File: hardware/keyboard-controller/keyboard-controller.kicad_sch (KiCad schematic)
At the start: 17 parts, among them J1 Debug_Pins, SW1 RESET, SW2 MODE_SEL, U1 Pico, U2 MCP4921

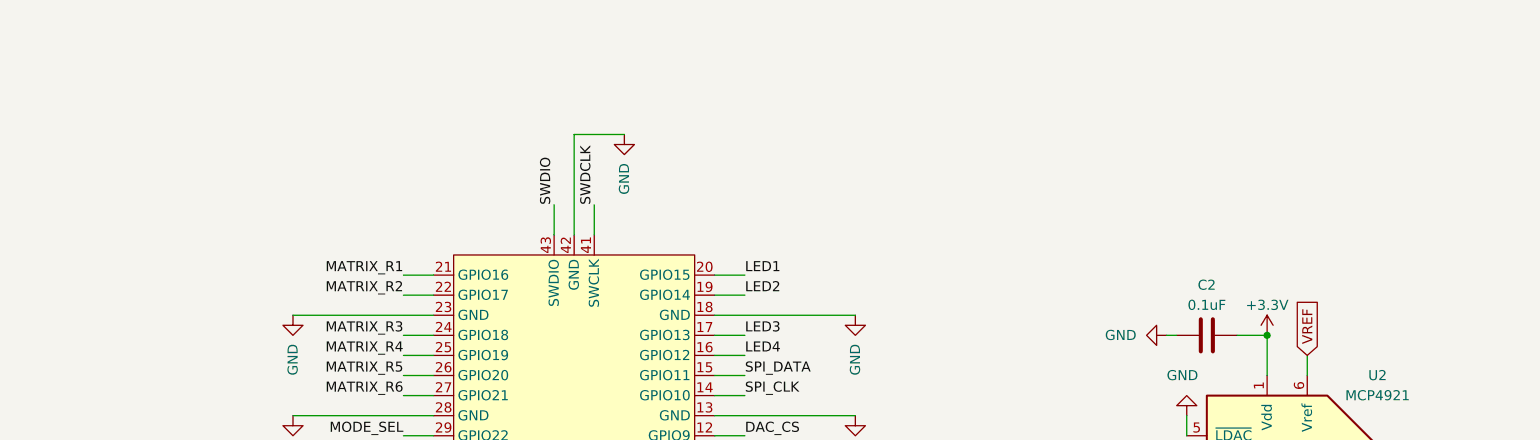
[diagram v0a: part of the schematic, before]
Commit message: Completed schematic rev1. Started placing pcb
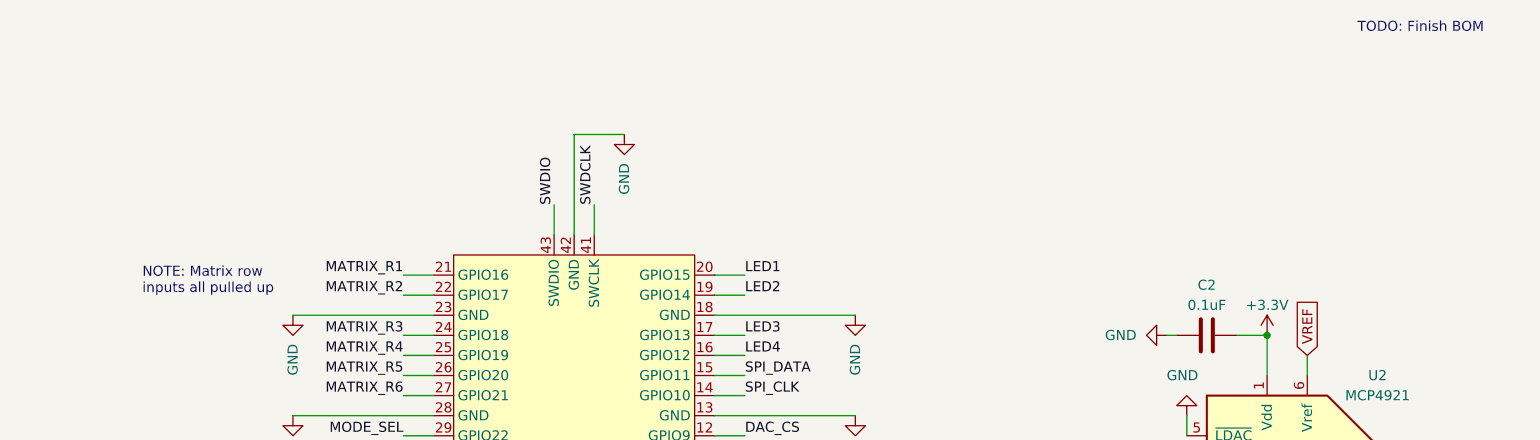
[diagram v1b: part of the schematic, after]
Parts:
- D1, D2, D3, D4, D5: footprint (none) -> LED_THT:LED_D5.0mm
- R1, R2, R3, R4, R5: footprint (none) -> Royal_Ohm_Resistors:R_Axial_DIN0207_L6.8mm_D2.5mm_P10.16mm_Horizontal
- SW1: footprint (none) -> Button_Switch_THT:SW_PUSH_6mm; Manufacturer (none) -> WEALTH METAL; Manufacturer Part No. (none) -> Tact Switch 6x6mm 5mm; Supplier Part No. (none) -> A-5127
- SW2: footprint (none) -> Wealth_Metal_Switches:Slide_Switch_SPDT_SS12F44G5; Manufacturer (none) -> WEALTH METAL; Manufacturer Part No. (none) -> SS12F44G5; Supplier Part No. (none) -> A-659
- U1: footprint RPi_Pico:RPi_Pico_SMD_TH -> MCU_RaspberryPi_and_Boards:RPi_Pico_SMD_TH
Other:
- note added: "NOTE: Matrix row inputs all pulled up"
- note added: "TODO: Finish BOM"

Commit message: Completed initial pcb design
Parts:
- added H1, H2, H3, H4: MountingHole, MountingHole:MountingHole_3.2mm_M3, symbol Mechanical:MountingHole
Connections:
- net GND: now also J1.4 (Pin_4); no longer J1.2 (Pin_2)
- net SERCLK: now also J1.2 (Pin_2); no longer J1.4 (Pin_4)
- net SERDATA: now also J1.1 (Pin_1); no longer J1.5 (Pin_5)
- net SWDCLK: now also J1.3 (Pin_3); no longer J1.1 (Pin_1)
- net SWDIO: now also J1.5 (Pin_5); no longer J1.3 (Pin_3)
- net +3V3 renamed +3.3V

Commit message: Added more text detail to PCB. Completed more of BOM
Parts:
- D1: Manufacturer (none) -> Tayda; Manufacturer Part No. (none) -> LED 5mm Green; Supplier Part No. (none) -> A-1553
- D2, D3, D4, D5: Manufacturer (none) -> Cree LED; Manufacturer Part No. (none) -> C503B-RAN-CZ0C0AA1; Notes (none) -> Standard 5mm Red LED; Supplier Tayda -> Mouser; Supplier Part No. (none) -> 941-C503BRANCZ0C0AA1
- H1, H2, H3, H4: Manufacturer (none) -> N/A; Manufacturer Part No. (none) -> N/A; Notes (none) -> N/A; Supplier (none) -> N/A; Supplier Part No. (none) -> N/A
- J1: Manufacturer (none) -> GTK; Manufacturer Part No. (none) -> PHSS05G10; Supplier Part No. (none) -> A-5775
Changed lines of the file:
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@@
+      (effects (font (size 1.27 1.27)) hide)
+    )
+    (property "Manufacturer" "Tayda" (id 5) (at 111.76 119.38 0)
+      (effects (font (size 1.27 1.27)) hide)
+    )
+    (property "Manufacturer Part No." "LED 5mm Green" (id 6) (at 111.76 119.38 0)
+      (effects (font (size 1.27 1.27)) hide)
+    )
+    (property "Supplier Part No." "A-1553" (id 7) (at 111.76 119.38 0)
       (effects (font (size 1.27 1.27)) hide)
     )
@@
       (effects (font (size 1.27 1.27)) hide)
     )
+    (property "Manufacturer" "N/A" (id 4) (at 254 148.59 0)
+      (effects (font (size 1.27 1.27)) hide)
+    )
+    (property "Manufacturer Part No." "N/A" (id 5) (at 254 148.59 0)
+      (effects (font (size 1.27 1.27)) hide)
+    )
+    (property "Notes" "N/A" (id 6) (at 254 148.59 0)
+      (effects (font (size 1.27 1.27)) hide)
+    )
+    (property "Supplier" "N/A" (id 7) (at 254 148.59 0)
+      (effects (font (size 1.27 1.27)) hide)
+    )
+    (property "Supplier Part No." "N/A" (id 8) (at 254 148.59 0)
+      (effects (font (size 1.27 1.27)) hide)
+    )
   )
   (symbol (lib_id "Mechanical:MountingHole") (at 232.41 148.59 0) (unit 1)
@@
       (effects (font (size 1.27 1.27)) hide)
     )
+    (property "Manufacturer" "N/A" (id 4) (at 232.41 148.59 0)
+      (effects (font (size 1.27 1.27)) hide)
+    )
+    (property "Manufacturer Part No." "N/A" (id 5) (at 232.41 148.59 0)
+      (effects (font (size 1.27 1.27)) hide)
+    )
+    (property "Notes" "N/A" (id 6) (at 232.41 148.59 0)
+      (effects (font (size 1.27 1.27)) hide)
+    )
+    (property "Supplier" "N/A" (id 7) (at 232.41 148.59 0)
+      (effects (font (size 1.27 1.27)) hide)
+    )
+    (property "Supplier Part No." "N/A" (id 8) (at 232.41 148.59 0)
+      (effects (font (size 1.27 1.27)) hide)
+    )
   )
   (symbol (lib_id "Device:R") (at 124.46 135.89 90) (unit 1)
@@
       (effects (font (size 1.27 1.27)) hide)
     )
-    (property "Supplier" "Tayda" (id 4) (at 113.03 167.64 0)
+    (property "Supplier" "Mouser" (id 4) (at 113.03 167.64 0)
+      (effects (font (size 1.27 1.27)) hide)
+    )
+    (property "Manufacturer" "Cree LED" (id 5) (at 113.03 167.64 0)
+      (effects (font (size 1.27 1.27)) hide)
+    )
+    (property "Manufacturer Part No." "C503B-RAN-CZ0C0AA1 " (id 6) (at 113.03 167.64 0)
+      (effects (font (size 1.27 1.27)) hide)
+    )
+    (property "Notes" "Standard 5mm Red LED" (id 7) (at 113.03 167.64 0)
+      (effects (font (size 1.27 1.27)) hide)
+    )
+    (property "Supplier Part No." "941-C503BRANCZ0C0AA1 " (id 8) (at 113.03 167.64 0)
       (effects (font (size 1.27 1.27)) hide)
     )
@@
       (effects (font (size 1.27 1.27)) hide)
     )
+    (property "Manufacturer" "N/A" (id 4) (at 254 158.75 0)
+      (effects (font (size 1.27 1.27)) hide)
+    )
+    (property "Manufacturer Part No." "N/A" (id 5) (at 254 158.75 0)
+      (effects (font (size 1.27 1.27)) hide)
+    )
+    (property "Notes" "N/A" (id 6) (at 254 158.75 0)
+      (effects (font (size 1.27 1.27)) hide)
+    )
+    (property "Supplier" "N/A" (id 7) (at 254 158.75 0)
+      (effects (font (size 1.27 1.27)) hide)
+    )
+    (property "Supplier Part No." "N/A" (id 8) (at 254 158.75 0)
+      (effects (font (size 1.27 1.27)) hide)
+    )
   )
   (symbol (lib_id "power:GND") (at 130.81 96.52 0) (unit 1)
@@
       (effects (font (size 1.27 1.27)) hide)
     )
+    (property "Manufacturer" "N/A" (id 4) (at 232.41 158.75 0)
+      (effects (font (size 1.27 1.27)) hide)
+    )
+    (property "Manufacturer Part No." "N/A" (id 5) (at 232.41 158.75 0)
+      (effects (font (size 1.27 1.27)) hide)
+    )
+    (property "Notes" "N/A" (id 6) (at 232.41 158.75 0)
+      (effects (font (size 1.27 1.27)) hide)
+    )
+    (property "Supplier" "N/A" (id 7) (at 232.41 158.75 0)
+      (effects (font (size 1.27 1.27)) hide)
+    )
+    (property "Supplier Part No." "N/A" (id 8) (at 232.41 158.75 0)
+      (effects (font (size 1.27 1.27)) hide)
+    )
   )
   (symbol (lib_id "power:GND") (at 187.96 57.15 0) (mirror y) (unit 1)
@@
       (effects (font (size 1.27 1.27)) hide)
     )
-    (property "Supplier" "Tayda" (id 4) (at 113.03 184.15 0)
+    (property "Supplier" "Mouser" (id 4) (at 113.03 184.15 0)
+      (effects (font (size 1.27 1.27)) hide)
+    )
+    (property "Manufacturer" "Cree LED" (id 5) (at 113.03 184.15 0)
+      (effects (font (size 1.27 1.27)) hide)
+    )
+    (property "Manufacturer Part No." "C503B-RAN-CZ0C0AA1 " (id 6) (at 113.03 184.15 0)
+      (effects (font (size 1.27 1.27)) hide)
+    )
+    (property "Notes" "Standard 5mm Red LED" (id 7) (at 113.03 184.15 0)
+      (effects (font (size 1.27 1.27)) hide)
+    )
+    (property "Supplier Part No." "941-C503BRANCZ0C0AA1 " (id 8) (at 113.03 184.15 0)
       (effects (font (size 1.27 1.27)) hide)
     )
@@
       (effects (font (size 1.27 1.27)) hide)
     )
-    (property "Supplier" "Tayda" (id 4) (at 111.76 151.13 0)
+    (property "Supplier" "Mouser" (id 4) (at 111.76 151.13 0)
+      (effects (font (size 1.27 1.27)) hide)
+    )
+    (property "Manufacturer" "Cree LED" (id 5) (at 111.76 151.13 0)
+      (effects (font (size 1.27 1.27)) hide)
+    )
+    (property "Manufacturer Part No." "C503B-RAN-CZ0C0AA1 " (id 6) (at 111.76 151.13 0)
+      (effects (font (size 1.27 1.27)) hide)
+    )
+    (property "Notes" "Standard 5mm Red LED" (id 7) (at 111.76 151.13 0)
+      (effects (font (size 1.27 1.27)) hide)
+    )
+    (property "Supplier Part No." "941-C503BRANCZ0C0AA1 " (id 8) (at 111.76 151.13 0)
       (effects (font (size 1.27 1.27)) hide)
     )
@@
       (effects (font (size 1.27 1.27)) hide)
     )
+    (property "Manufacturer" "GTK" (id 5) (at 35.56 168.91 0)
+      (effects (font (size 1.27 1.27)) hide)
+    )
+    (property "Manufacturer Part No." "PHSS05G10" (id 6) (at 35.56 168.91 0)
+      (effects (font (size 1.27 1.27)) hide)
+    )
+    (property "Supplier Part No." "A-5775" (id 7) (at 35.56 168.91 0)
+      (effects (font (size 1.27 1.27)) hide)
+    )
     (pin "1")
     (pin "2")
@@
       (effects (font (size 1.27 1.27)) hide)
     )
-    (property "Supplier" "Tayda" (id 4) (at 111.76 135.89 0)
+    (property "Supplier" "Mouser" (id 4) (at 111.76 135.89 0)
+      (effects (font (size 1.27 1.27)) hide)
+    )
+    (property "Manufacturer" "Cree LED" (id 5) (at 111.76 135.89 0)
+      (effects (font (size 1.27 1.27)) hide)
+    )
+    (property "Manufacturer Part No." "C503B-RAN-CZ0C0AA1 " (id 6) (at 111.76 135.89 0)
+      (effects (font (size 1.27 1.27)) hide)
+    )
+    (property "Notes" "Standard 5mm Red LED" (id 7) (at 111.76 135.89 0)
+      (effects (font (size 1.27 1.27)) hide)
+    )
+    (property "Supplier Part No." "941-C503BRANCZ0C0AA1 " (id 8) (at 111.76 135.89 0)
       (effects (font (size 1.27 1.27)) hide)
     )
@@
     )
     (path "/e62cebf1-8b49-4ab0-9851-a340dc04dbf1/4d9f0d5e-90b9-4ffb-9be8-20dc6a9551ac"
-      (reference "U4") (unit 1) (value "TL431LP") (footprint "Package_TO_SOT_THT:TO-92_Inline")
+      (reference "U4") (unit 1) (value "TL431") (footprint "Package_TO_SOT_THT:TO-92_Inline")
     )
     (path "/e62cebf1-8b49-4ab0-9851-a340dc04dbf1/ffff614e-784d-4805-a807-3794da1928aa"

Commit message: Completed BOM
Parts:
- R1, R2, R3, R4, R5: Manufacturer (none) -> Royal Ohm; Manufacturer Part No. (none) -> MF0W4FF4700A50; Supplier Part No. (none) -> A-2247
- U1: Manufacturer (none) -> Raspberry Pi; Manufacturer Part No. (none) -> SC0915; Supplier (none) -> Digikey; Supplier Part No. (none) -> 2648-SC0915CT-ND
- U2: Manufacturer (none) -> Microchip Technology / Atmel; Manufacturer Part No. (none) -> MCP4921-E/P; Supplier (none) -> Mouser; Supplier Part No. (none) -> 579-MCP4921-E/P
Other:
- note removed: "TODO: Finish BOM"
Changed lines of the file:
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@@
-    (effects (font (size 1.27 1.27)) (justify left bottom))
-  )
-  (text "TODO: Finish BOM" (at 251.46 8.89 0)
     (effects (font (size 1.27 1.27)) (justify left bottom))
   )
@@
       (effects (font (size 1.27 1.27)) hide)
     )
+    (property "Manufacturer" "Royal Ohm" (id 5) (at 125.73 167.64 0)
+      (effects (font (size 1.27 1.27)) hide)
+    )
+    (property "Manufacturer Part No." "MF0W4FF4700A50" (id 6) (at 125.73 167.64 0)
+      (effects (font (size 1.27 1.27)) hide)
+    )
+    (property "Supplier Part No." "A-2247" (id 7) (at 125.73 167.64 0)
+      (effects (font (size 1.27 1.27)) hide)
+    )
     (pin "1")
     (pin "2")
@@
     )
     (property "Datasheet" "" (id 3) (at 152.4 63.5 0)
+      (effects (font (size 1.27 1.27)) hide)
+    )
+    (property "Manufacturer" "Raspberry Pi" (id 4) (at 152.4 63.5 0)
+      (effects (font (size 1.27 1.27)) hide)
+    )
+    (property "Manufacturer Part No." "SC0915" (id 5) (at 152.4 63.5 0)
+      (effects (font (size 1.27 1.27)) hide)
+    )
+    (property "Supplier" "Digikey" (id 6) (at 152.4 63.5 0)
+      (effects (font (size 1.27 1.27)) hide)
+    )
+    (property "Supplier Part No." "2648-SC0915CT-ND" (id 7) (at 152.4 63.5 0)
       (effects (font (size 1.27 1.27)) hide)
     )
@@
       (effects (font (size 1.27 1.27)) hide)
     )
+    (property "Manufacturer" "Royal Ohm" (id 5) (at 124.46 135.89 0)
+      (effects (font (size 1.27 1.27)) hide)
+    )
+    (property "Manufacturer Part No." "MF0W4FF4700A50" (id 6) (at 124.46 135.89 0)
+      (effects (font (size 1.27 1.27)) hide)
+    )
+    (property "Supplier Part No." "A-2247" (id 7) (at 124.46 135.89 0)
+      (effects (font (size 1.27 1.27)) hide)
+    )
     (pin "1")
     (pin "2")
@@
     )
     (property "Supplier" "Tayda" (id 4) (at 125.73 184.15 0)
+      (effects (font (size 1.27 1.27)) hide)
+    )
+    (property "Manufacturer" "Royal Ohm" (id 5) (at 125.73 184.15 0)
+      (effects (font (size 1.27 1.27)) hide)
+    )
+    (property "Manufacturer Part No." "MF0W4FF4700A50" (id 6) (at 125.73 184.15 0)
+      (effects (font (size 1.27 1.27)) hide)
+    )
+    (property "Supplier Part No." "A-2247" (id 7) (at 125.73 184.15 0)
       (effects (font (size 1.27 1.27)) hide)
     )
@@
       (effects (font (size 1.27 1.27)) hide)
     )
+    (property "Manufacturer" "Royal Ohm" (id 5) (at 124.46 119.38 0)
+      (effects (font (size 1.27 1.27)) hide)
+    )
+    (property "Manufacturer Part No." "MF0W4FF4700A50" (id 6) (at 124.46 119.38 0)
+      (effects (font (size 1.27 1.27)) hide)
+    )
+    (property "Supplier Part No." "A-2247" (id 7) (at 124.46 119.38 0)
+      (effects (font (size 1.27 1.27)) hide)
+    )
     (pin "1")
     (pin "2")
@@
     )
     (property "Datasheet" "http://ww1.microchip.com/downloads/en/DeviceDoc/22248a.pdf" (id 3) (at 265.43 64.77 0)
+      (effects (font (size 1.27 1.27)) hide)
+    )
+    (property "Manufacturer" "Microchip Technology / Atmel " (id 4) (at 240.03 62.23 0)
+      (effects (font (size 1.27 1.27)) hide)
+    )
+    (property "Manufacturer Part No." "MCP4921-E/P " (id 5) (at 240.03 62.23 0)
+      (effects (font (size 1.27 1.27)) hide)
+    )
+    (property "Supplier" "Mouser" (id 6) (at 240.03 62.23 0)
+      (effects (font (size 1.27 1.27)) hide)
+    )
+    (property "Supplier Part No." " 579-MCP4921-E/P" (id 7) (at 240.03 62.23 0)
       (effects (font (size 1.27 1.27)) hide)
     )
@@
       (effects (font (size 1.27 1.27)) hide)
     )
+    (property "Manufacturer" "Royal Ohm" (id 5) (at 124.46 151.13 0)
+      (effects (font (size 1.27 1.27)) hide)
+    )
+    (property "Manufacturer Part No." "MF0W4FF4700A50" (id 6) (at 124.46 151.13 0)
+      (effects (font (size 1.27 1.27)) hide)
+    )
+    (property "Supplier Part No." "A-2247" (id 7) (at 124.46 151.13 0)
+      (effects (font (size 1.27 1.27)) hide)
+    )
     (pin "1")
     (pin "2")
@@
     )
     (path "/679aab57-7a27-4204-9526-edba148bc933/2328e1e7-2c8f-4614-bec5-81b9e4e06ef8"
-      (reference "R11") (unit 1) (value "1k") (footprint "Royal_Ohm_Resistors:R_Axial_DIN0207_L6.8mm_D2.5mm_P10.16mm_Horizontal")
+      (reference "R11") (unit 1) (value "1K") (footprint "Royal_Ohm_Resistors:R_Axial_DIN0207_L6.8mm_D2.5mm_P10.16mm_Horizontal")
     )
     (path "/679aab57-7a27-4204-9526-edba148bc933/aac74ad6-9355-4807-8b76-1d0d3f5a88f2"
